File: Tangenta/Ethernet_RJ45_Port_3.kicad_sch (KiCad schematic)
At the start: 1 part, among them J7 HY911130A

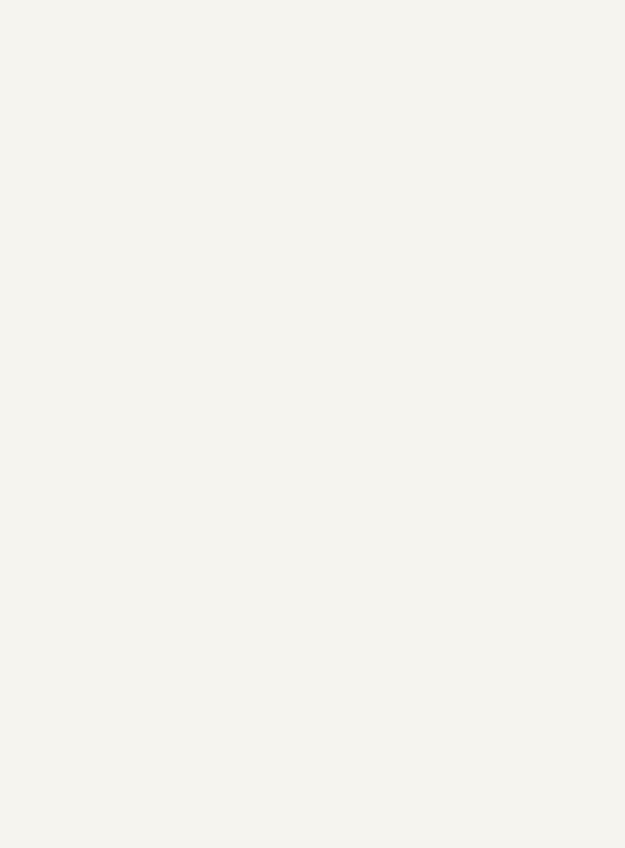
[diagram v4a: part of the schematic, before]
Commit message: Ethernet Switch schematic done, ports TBD...
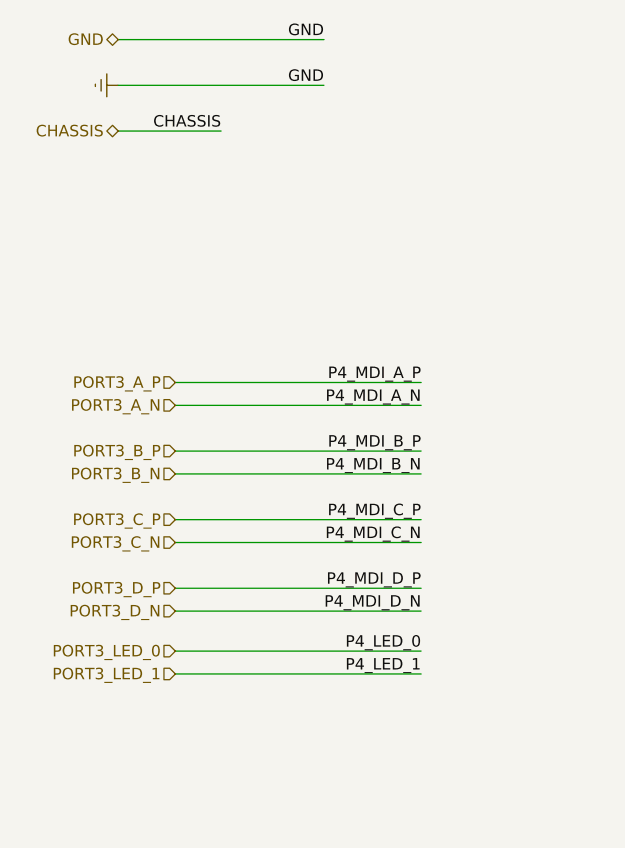
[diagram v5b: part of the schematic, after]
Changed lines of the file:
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@@
   (no_connect (at 165.735 100.965))
   (no_connect (at 140.335 93.345))
+  (wire (pts (xy 59.055 72.39) (xy 31.75 72.39))
+    (stroke (width 0) (type default))
+  )
+  (wire (pts (xy 59.055 80.01) (xy 31.75 80.01))
+    (stroke (width 0) (type default))
+  )
+  (wire (pts (xy 48.26 19.05) (xy 25.4 19.05))
+    (stroke (width 0) (type default))
+  )
+  (wire (pts (xy 59.055 89.535) (xy 31.75 89.535))
+    (stroke (width 0) (type default))
+  )
+  (wire (pts (xy 25.4 29.21) (xy 36.83 29.21))
+    (stroke (width 0) (type default))
+  )
+  (wire (pts (xy 48.26 24.13) (xy 25.4 24.13))
+    (stroke (width 0) (type default))
+  )
+  (wire (pts (xy 59.055 57.15) (xy 31.75 57.15))
+    (stroke (width 0) (type default))
+  )
+  (wire (pts (xy 59.055 59.69) (xy 31.75 59.69))
+    (stroke (width 0) (type default))
+  )
+  (wire (pts (xy 59.055 86.995) (xy 31.75 86.995))
+    (stroke (width 0) (type default))
+  )
+  (wire (pts (xy 59.055 82.55) (xy 31.75 82.55))
+    (stroke (width 0) (type default))
+  )
+  (wire (pts (xy 59.055 64.77) (xy 31.75 64.77))
+    (stroke (width 0) (type default))
+  )
+  (wire (pts (xy 59.055 74.93) (xy 31.75 74.93))
+    (stroke (width 0) (type default))
+  )
+  (wire (pts (xy 59.055 67.31) (xy 31.75 67.31))
+    (stroke (width 0) (type default))
+  )
+  (label "P4_MDI_C_N" (at 59.055 74.93 180) (fields_autoplaced)
+    (effects (font (size 1.27 1.27)) (justify right bottom))
+  )
+  (label "GND" (at 48.26 24.13 180) (fields_autoplaced)
+    (effects (font (size 1.27 1.27)) (justify right bottom))
+  )
+  (label "P4_MDI_D_P" (at 59.055 80.01 180) (fields_autoplaced)
+    (effects (font (size 1.27 1.27)) (justify right bottom))
+  )
+  (label "GND" (at 48.26 19.05 180) (fields_autoplaced)
+    (effects (font (size 1.27 1.27)) (justify right bottom))
+  )
+  (label "P4_MDI_D_N" (at 59.055 82.55 180) (fields_autoplaced)
+    (effects (font (size 1.27 1.27)) (justify right bottom))
+  )
+  (label "CHASSIS" (at 36.83 29.21 180) (fields_autoplaced)
+    (effects (font (size 1.27 1.27)) (justify right bottom))
+  )
+  (label "P4_LED_0" (at 59.055 86.995 180) (fields_autoplaced)
+    (effects (font (size 1.27 1.27)) (justify right bottom))
+  )
+  (label "P4_MDI_C_P" (at 59.055 72.39 180) (fields_autoplaced)
+    (effects (font (size 1.27 1.27)) (justify right bottom))
+  )
+  (label "P4_MDI_B_P" (at 59.055 64.77 180) (fields_autoplaced)
+    (effects (font (size 1.27 1.27)) (justify right bottom))
+  )
+  (label "P4_MDI_B_N" (at 59.055 67.31 180) (fields_autoplaced)
+    (effects (font (size 1.27 1.27)) (justify right bottom))
+  )
+  (label "P4_LED_1" (at 59.055 89.535 180) (fields_autoplaced)
+    (effects (font (size 1.27 1.27)) (justify right bottom))
+  )
+  (label "P4_MDI_A_N" (at 59.055 59.69 180) (fields_autoplaced)
+    (effects (font (size 1.27 1.27)) (justify right bottom))
+  )
+  (label "P4_MDI_A_P" (at 59.055 57.15 180) (fields_autoplaced)
+    (effects (font (size 1.27 1.27)) (justify right bottom))
+  )
+  (hierarchical_label "PORT3_D_N" (shape input) (at 31.75 82.55 180) (fields_autoplaced)
+    (effects (font (size 1.27 1.27)) (justify right))
+  )
+  (hierarchical_label "PORT3_A_N" (shape input) (at 31.75 59.69 180) (fields_autoplaced)
+    (effects (font (size 1.27 1.27)) (justify right))
+  )
+  (hierarchical_label "GND" (shape bidirectional) (at 25.4 19.05 180) (fields_autoplaced)
+    (effects (font (size 1.27 1.27)) (justify right))
+  )
+  (hierarchical_label "PORT3_A_P" (shape input) (at 31.75 57.15 180) (fields_autoplaced)
+    (effects (font (size 1.27 1.27)) (justify right))
+  )
+  (hierarchical_label "CHASSIS" (shape bidirectional) (at 25.4 29.21 180) (fields_autoplaced)
+    (effects (font (size 1.27 1.27)) (justify right))
+  )
+  (hierarchical_label "PORT3_C_N" (shape input) (at 31.75 74.93 180) (fields_autoplaced)
+    (effects (font (size 1.27 1.27)) (justify right))
+  )
+  (hierarchical_label "PORT3_C_P" (shape input) (at 31.75 72.39 180) (fields_autoplaced)
+    (effects (font (size 1.27 1.27)) (justify right))
+  )
+  (hierarchical_label "PORT3_B_N" (shape input) (at 31.75 67.31 180) (fields_autoplaced)
+    (effects (font (size 1.27 1.27)) (justify right))
+  )
+  (hierarchical_label "PORT3_B_P" (shape input) (at 31.75 64.77 180) (fields_autoplaced)
+    (effects (font (size 1.27 1.27)) (justify right))
+  )
+  (hierarchical_label "PORT3_LED_1" (shape input) (at 31.75 89.535 180) (fields_autoplaced)
+    (effects (font (size 1.27 1.27)) (justify right))
+  )
+  (hierarchical_label "PORT3_D_P" (shape input) (at 31.75 80.01 180) (fields_autoplaced)
+    (effects (font (size 1.27 1.27)) (justify right))
+  )
+  (hierarchical_label "PORT3_LED_0" (shape input) (at 31.75 86.995 180) (fields_autoplaced)
+    (effects (font (size 1.27 1.27)) (justify right))
+  )
+  (symbol (lib_id "power:GNDREF") (at 25.4 24.13 270) (mirror x) (unit 1)
+    (in_bom yes) (on_board yes) (dnp no) (fields_autoplaced)
+    (property "Reference" "#PWR013" (at 19.05 24.13 0)
+      (effects (font (size 1.27 1.27)) hide)
+    )
+    (property "Value" "GNDREF" (at 21.59 24.13 90)
+      (effects (font (size 1.27 1.27)) (justify right) hide)
+    )
+    (property "Footprint" "" (at 25.4 24.13 0)
+      (effects (font (size 1.27 1.27)) hide)
+    )
+    (property "Datasheet" "" (at 25.4 24.13 0)
+      (effects (font (size 1.27 1.27)) hide)
+    )
+    (pin "1")
+    (instances
+      (project "Tangenta"
+        (path "/358d1bcf-7599-4352-8c4d-baa18a5f09e6/d6c05402-162e-441f-bed8-be7996260fb4"
+          (reference "#PWR013") (unit 1)
+        )
+        (path "/358d1bcf-7599-4352-8c4d-baa18a5f09e6/9b1f6f94-444c-4c59-8de9-290bde336856"
+          (reference "#PWR050") (unit 1)
+        )
+        (path "/358d1bcf-7599-4352-8c4d-baa18a5f09e6/9b1f6f94-444c-4c59-8de9-290bde336856/04648235-6c5e-4915-ab80-8fea22048f3c"
+          (reference "#PWR050") (unit 1)
+        )
+        (path "/358d1bcf-7599-4352-8c4d-baa18a5f09e6/2bb52479-7b35-496d-9807-27e706c6ef7b"
+          (reference "#PWR059") (unit 1)
+        )
+        (path "/358d1bcf-7599-4352-8c4d-baa18a5f09e6/2bb52479-7b35-496d-9807-27e706c6ef7b/c653b84e-94ee-4be9-b47c-8c767f88973e"
+          (reference "#PWR059") (unit 1)
+        )
+        (path "/358d1bcf-7599-4352-8c4d-baa18a5f09e6/2bb52479-7b35-496d-9807-27e706c6ef7b/5dd23ea2-ad33-4f2c-a45e-3d59d95f0b2c"
+          (reference "#PWR067") (unit 1)
+        )
+      )
+    )
+  )
   (symbol (lib_id "RJ45_MAGJACK:HY911130A") (at 153.035 99.695 0) (unit 1)
     (in_bom yes) (on_board yes) (dnp no)

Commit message: Ethernet, current progress...
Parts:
- added C1: 100nF, Capacitor_SMD:C_0402_1005Metric, symbol Device:C_Small
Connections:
- net CHASSIS: now also J7.15 (SH), J7.16 (SH)
- net GNDREF: now also J7.10, J7.12, J7.13, C1.2
- net at J7.1: now also C1.1
- no-connect marks 16 -> 0

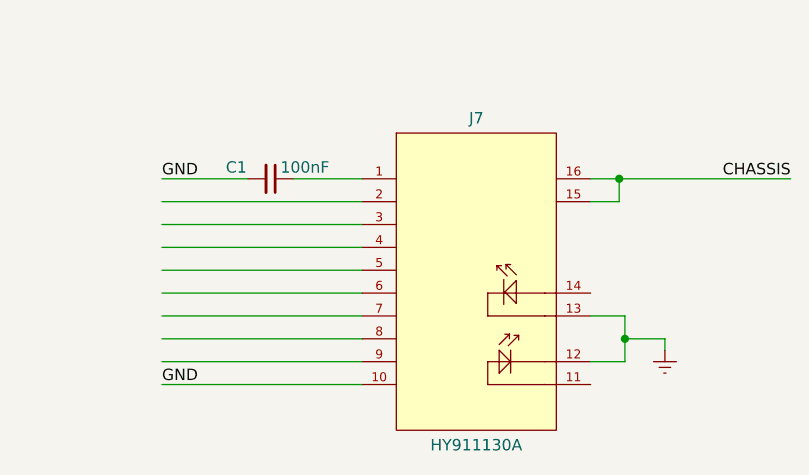
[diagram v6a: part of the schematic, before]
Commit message: Ethernet, SFP to be done...
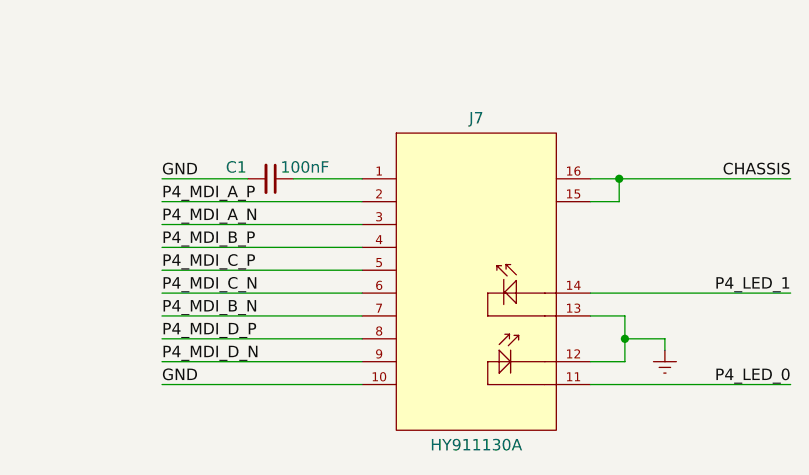
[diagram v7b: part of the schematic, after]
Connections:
- net PORT3_A_N: now also J7.3
- net PORT3_A_P: now also J7.2
- net PORT3_B_N: now also J7.7
- net PORT3_B_P: now also J7.4
- net PORT3_C_N: now also J7.6
- net PORT3_C_P: now also J7.5
- net PORT3_D_N: now also J7.9
- net PORT3_D_P: now also J7.8
- net PORT3_LED_0: now also J7.11
- net PORT3_LED_1: now also J7.14
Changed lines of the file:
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@@
+    (stroke (width 0) (type default))
+  )
+  (wire (pts (xy 160.02 93.345) (xy 182.245 93.345))
     (stroke (width 0) (type default))
   )
@@
   )
   (wire (pts (xy 59.055 80.01) (xy 31.75 80.01))
+    (stroke (width 0) (type default))
+  )
+  (wire (pts (xy 160.02 83.185) (xy 182.245 83.185))
     (stroke (width 0) (type default))
   )
@@
     (stroke (width 0) (type default))
   )
+  (label "P4_MDI_C_P" (at 112.395 80.645 0) (fields_autoplaced)
+    (effects (font (size 1.27 1.27)) (justify left bottom))
+  )
+  (label "P4_MDI_D_N" (at 112.395 90.805 0) (fields_autoplaced)
+    (effects (font (size 1.27 1.27)) (justify left bottom))
+  )
+  (label "P4_MDI_A_N" (at 112.395 75.565 0) (fields_autoplaced)
+    (effects (font (size 1.27 1.27)) (justify left bottom))
+  )
   (label "P4_MDI_C_N" (at 59.055 74.93 180) (fields_autoplaced)
     (effects (font (size 1.27 1.27)) (justify right bottom))
@@
     (effects (font (size 1.27 1.27)) (justify right bottom))
   )
+  (label "P4_MDI_A_P" (at 112.395 73.025 0) (fields_autoplaced)
+    (effects (font (size 1.27 1.27)) (justify left bottom))
+  )
   (label "P4_MDI_D_P" (at 59.055 80.01 180) (fields_autoplaced)
     (effects (font (size 1.27 1.27)) (justify right bottom))
+  )
+  (label "P4_MDI_C_N" (at 112.395 83.185 0) (fields_autoplaced)
+    (effects (font (size 1.27 1.27)) (justify left bottom))
   )
   (label "GND" (at 48.26 19.05 180) (fields_autoplaced)
@@
   (label "CHASSIS" (at 36.83 29.21 180) (fields_autoplaced)
     (effects (font (size 1.27 1.27)) (justify right bottom))
+  )
+  (label "P4_MDI_B_P" (at 112.395 78.105 0) (fields_autoplaced)
+    (effects (font (size 1.27 1.27)) (justify left bottom))
+  )
+  (label "P4_MDI_B_N" (at 112.395 85.725 0) (fields_autoplaced)
+    (effects (font (size 1.27 1.27)) (justify left bottom))
   )
   (label "P4_LED_0" (at 59.055 86.995 180) (fields_autoplaced)
@@
     (effects (font (size 1.27 1.27)) (justify right bottom))
   )
+  (label "P4_MDI_D_P" (at 112.395 88.265 0) (fields_autoplaced)
+    (effects (font (size 1.27 1.27)) (justify left bottom))
+  )
+  (label "P4_LED_1" (at 182.245 83.185 180) (fields_autoplaced)
+    (effects (font (size 1.27 1.27)) (justify right bottom))
+  )
   (label "P4_MDI_A_P" (at 59.055 57.15 180) (fields_autoplaced)
     (effects (font (size 1.27 1.27)) (justify right bottom))
   )
+  (label "P4_LED_0" (at 182.245 93.345 180) (fields_autoplaced)
+    (effects (font (size 1.27 1.27)) (justify right bottom))
+  )

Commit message: Libraries exported from global to project.
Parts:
- C1: symbol Device:C_Small -> CholaSymbolsPrjLib:C_Small
- J7: symbol RJ45_MAGJACK:HY911130A -> CholaSymbolsPrjLib:HY911130A
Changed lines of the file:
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@@
     )
   )
-  (symbol (lib_id "Device:C_Small") (at 124.46 70.485 270) (unit 1)
+  (symbol (lib_id "CholaSymbolsPrjLib:C_Small") (at 124.46 70.485 270) (unit 1)
     (in_bom yes) (on_board yes) (dnp no)
     (property "Reference" "C1" (at 120.65 69.215 90)
@@
     )
   )
-  (symbol (lib_id "RJ45_MAGJACK:HY911130A") (at 147.32 81.915 0) (unit 1)
+  (symbol (lib_id "CholaSymbolsPrjLib:HY911130A") (at 147.32 81.915 0) (unit 1)
     (in_bom yes) (on_board yes) (dnp no)
     (property "Reference" "J7" (at 147.32 63.754 0)
